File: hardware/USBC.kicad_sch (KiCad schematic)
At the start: 16 parts, among them J601 2305018-2, U601 CDSOT236-0504C, U602 CP2102N-A02-GQFN20

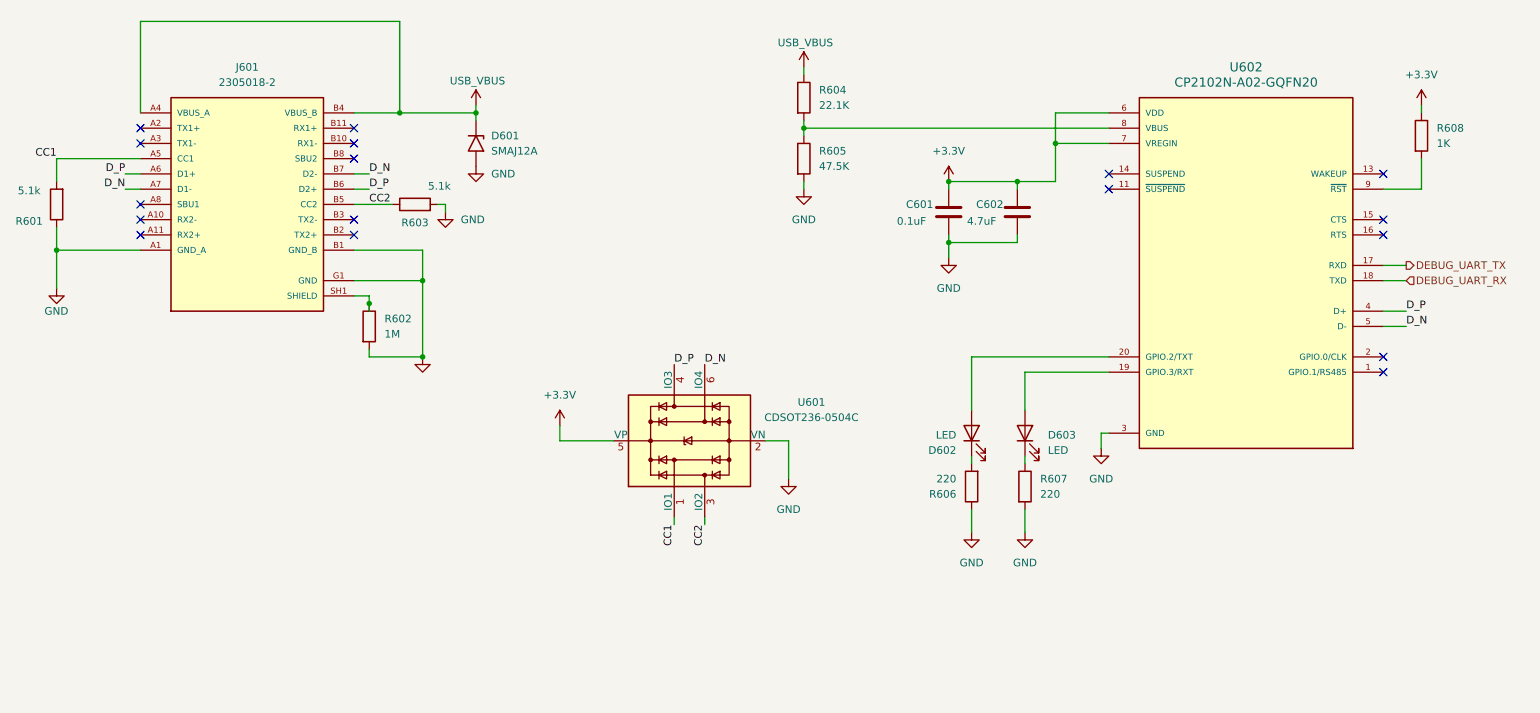
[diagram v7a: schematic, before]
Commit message: updated labels
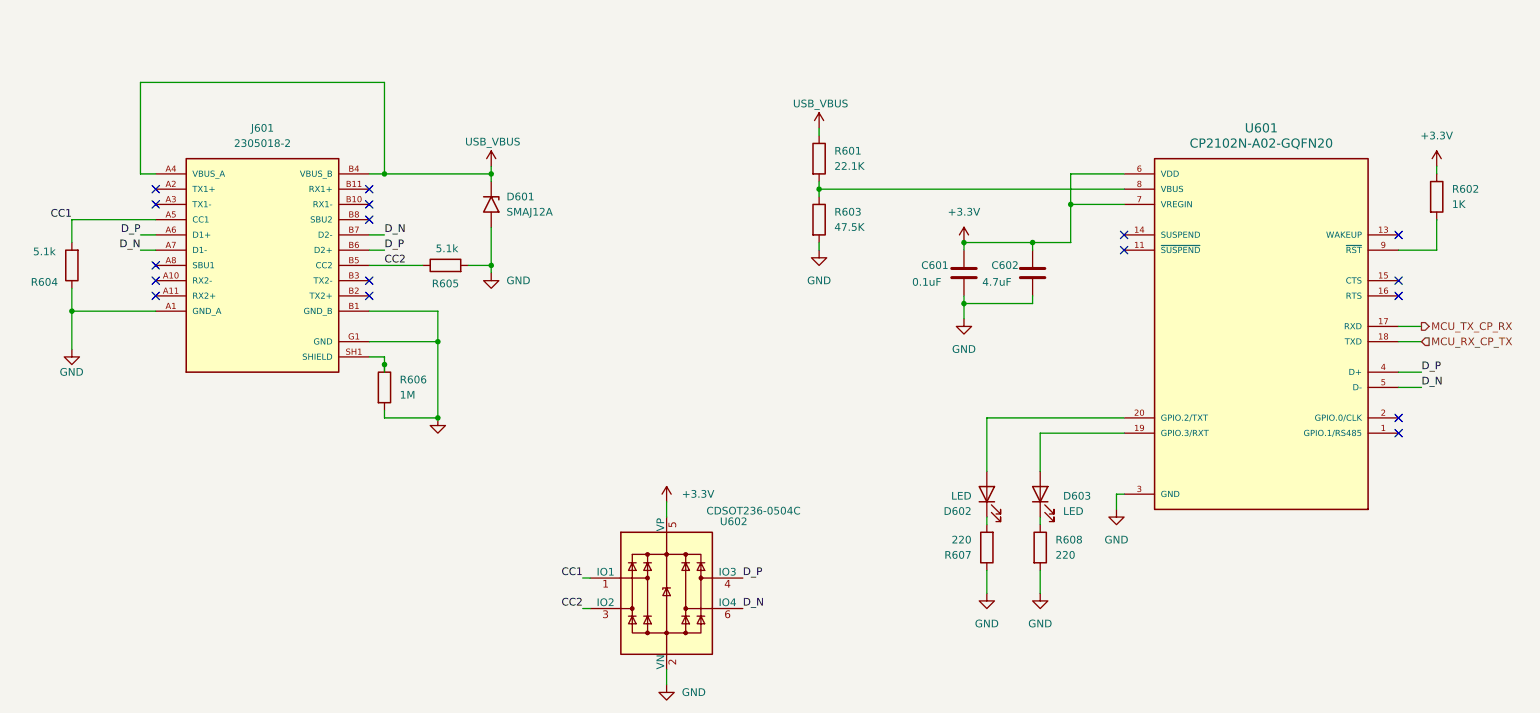
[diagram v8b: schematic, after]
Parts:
- renumbered R604 to R601, R608 to R602, R605 to R603, R601 to R604, R603 to R605, R602 to R606, R606 to R607, R607 to R608, U602 to U601, U601 to U602
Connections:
- net DEBUG_UART_RX renamed MCU_RX_CP_TX
- net DEBUG_UART_TX renamed MCU_TX_CP_RX
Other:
- moved on the sheet: C601, C602, D601, D602, D603, J601, R601, R602, R603, R604, R605, R606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
